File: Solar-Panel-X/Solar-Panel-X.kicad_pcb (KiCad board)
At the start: 6 copper layers, 48.4 x 48.4 mm, 81 parts, among them J1 FTS-105-01-L-DV-A, Q1 BSS138DWQ-7, Q2 MBT2222ADW1T1, Q3 BSS138DWQ-7, Q4 MBT2222ADW1T1, U1 BQ25570RGRR, U2 TSL2561

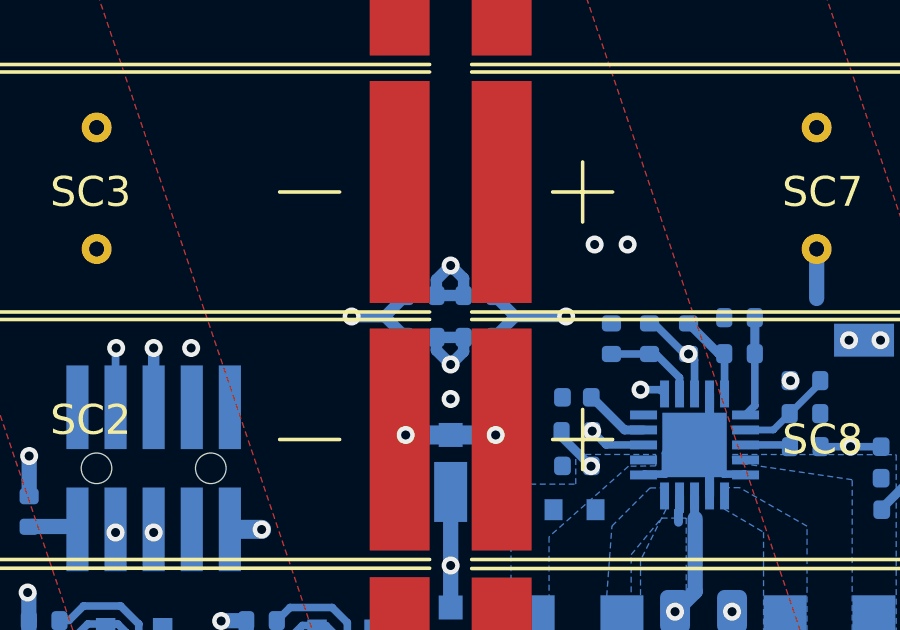
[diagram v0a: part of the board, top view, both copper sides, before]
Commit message: Modified coil resistor layout on X board
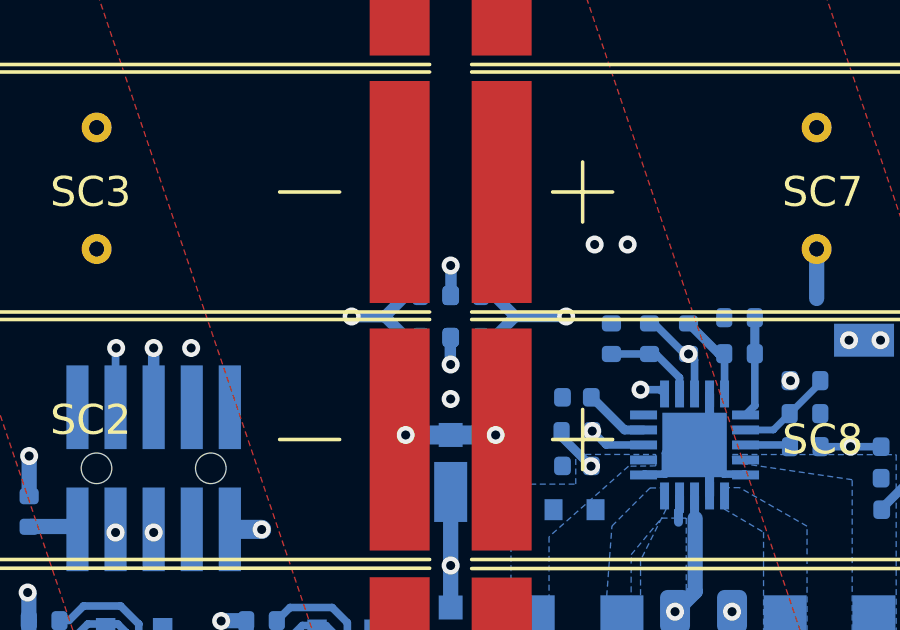
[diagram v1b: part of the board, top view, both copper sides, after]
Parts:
- moved R13 0.49 mm to (106.2, 67.0)
- moved R18 0.49 mm to (106.2, 65.6)
- moved R12 0.44 mm to (107.2, 67.0)
- moved R17 0.44 mm to (107.2, 65.6)
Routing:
- net COIL_N: track 17.1 -> 14.8 mm
- net COIL_P: track 17.3 -> 15.1 mm
- net /coil: track 13206.6 -> 13208.5 mm
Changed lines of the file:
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@@
   )
   (footprint "Resistor_SMD:R_0402_1005Metric" (layer "B.Cu")
-    (at 105.71397 65.6)
+    (at 106.2 65.6)
     (descr "Resistor SMD 0402 (1005 Metric), square (rectangular) end terminal, IPC_7351 nominal, (Body size source: IPC-SM-782 page 72, https://www.pcb-3d.com/wordpress/wp-content/uploads/ipc-sm-782a_amendment_1_and_2.pdf), generated with kicad-footprint-generator")
     (tags "resistor")
@@
   )
   (footprint "Resistor_SMD:R_0402_1005Metric" (layer "B.Cu")
-    (at 107.64225 65.6)
+    (at 107.2 65.6)
     (descr "Resistor SMD 0402 (1005 Metric), square (rectangular) end terminal, IPC_7351 nominal, (Body size source: IPC-SM-782 page 72, https://www.pcb-3d.com/wordpress/wp-content/uploads/ipc-sm-782a_amendment_1_and_2.pdf), generated with kicad-footprint-generator")
     (tags "resistor")
@@
   )
   (footprint "Resistor_SMD:R_0402_1005Metric" (layer "B.Cu")
-    (at 107.64225 66.997)
+    (at 107.2 67)
     (descr "Resistor SMD 0402 (1005 Metric), square (rectangular) end terminal, IPC_7351 nominal, (Body size source: IPC-SM-782 page 72, https://www.pcb-3d.com/wordpress/wp-content/uploads/ipc-sm-782a_amendment_1_and_2.pdf), generated with kicad-footprint-generator")
     (tags "resistor")
@@
   )
   (footprint "Resistor_SMD:R_0402_1005Metric" (layer "B.Cu")
-    (at 105.71397 66.997)
+    (at 106.2 66.997)
     (descr "Resistor SMD 0402 (1005 Metric), square (rectangular) end terminal, IPC_7351 nominal, (Body size source: IPC-SM-782 page 72, https://www.pcb-3d.com/wordpress/wp-content/uploads/ipc-sm-782a_amendment_1_and_2.pdf), generated with kicad-footprint-generator")
     (tags "resistor")
@@
   (segment (start 96.8 67.35) (end 96.8 66.7) (width 0.381) (layer "In2.Cu") (net 10))
   (segment (start 96.8 66.7) (end 98.9 64.6) (width 0.381) (layer "In2.Cu") (net 10))
-  (segment (start 106.22397 65.07603) (end 106.7 64.6) (width 0.381) (layer "B.Cu") (net 10))
-  (segment (start 106.22397 65.6) (end 107.13225 65.6) (width 0.381) (layer "B.Cu") (net 10))
+  (segment (start 106.71 64.61) (end 106.7 64.6) (width 0.1524) (layer "B.Cu") (net 10))
   (segment (start 96.8 67.35) (end 96.8 69.725) (width 0.381) (layer "B.Cu") (net 10))
-  (segment (start 106.7 64.6) (end 107.13225 65.03225) (width 0.381) (layer "B.Cu") (net 10))
-  (segment (start 107.13225 65.03225) (end 107.13225 65.6) (width 0.381) (layer "B.Cu") (net 10))
-  (segment (start 106.22397 65.6) (end 106.22397 65.07603) (width 0.381) (layer "B.Cu") (net 10))
+  (segment (start 106.71 65.6) (end 106.71 64.61) (width 0.381) (layer "B.Cu") (net 10))
   (via (at 106.7 67.9) (size 0.6) (drill 0.3) (layers "F.Cu" "B.Cu") (net 11))
   (via (at 96.8 73.5) (size 0.6) (drill 0.3) (layers "F.Cu" "B.Cu") (net 11))
@@
   (segment (start 99 67.9) (end 106.7 67.9) (width 0.381) (layer "In2.Cu") (net 11))
   (segment (start 96.8 73.5) (end 96.8 70.1) (width 0.381) (layer "In2.Cu") (net 11))
-  (segment (start 106.22397 66.997) (end 106.22397 67.42397) (width 0.381) (layer "B.Cu") (net 11))
-  (segment (start 106.22397 67.42397) (end 106.7 67.9) (width 0.381) (layer "B.Cu") (net 11))
-  (segment (start 107.13225 66.997) (end 107.13225 67.46775) (width 0.381) (layer "B.Cu") (net 11))
-  (segment (start 107.13225 67.46775) (end 106.7 67.9) (width 0.381) (layer "B.Cu") (net 11))
-  (segment (start 106.22397 66.997) (end 107.13225 66.997) (width 0.381) (layer "B.Cu") (net 11))
+  (segment (start 106.69 67.89) (end 106.7 67.9) (width 0.1524) (layer "B.Cu") (net 11))
+  (segment (start 106.69 67) (end 106.69 67.89) (width 0.381) (layer "B.Cu") (net 11))
   (segment (start 112.49644 70.081786) (end 111.408984 68.99433) (width 0.29972) (layer "B.Cu") (net 12))
   (segment (start 113.13 70.081786) (end 112.49644 70.081786) (width 0.29972) (layer "B.Cu") (net 12))
@@
   (segment (start 108.15525 66.997) (end 108.85225 66.3) (width 0.381) (layer "B.Cu") (net 22))
   (segment (start 103.4 66.3) (end 104.50397 66.3) (width 0.381) (layer "B.Cu") (net 22))
+  (segment (start 105.20397 66.997) (end 105.69 66.997) (width 0.381) (layer "B.Cu") (net 22))
   (segment (start 104.50397 66.3) (end 105.20397 65.6) (width 0.381) (layer "B.Cu") (net 22))
   (segment (start 103.4 66.3) (end 104.50697 66.3) (width 0.381) (layer "B.Cu") (net 22))
   (segment (start 108.85225 66.3) (end 110.55 66.3) (width 0.381) (layer "B.Cu") (net 22))
+  (segment (start 108.15225 65.6) (end 107.71 65.6) (width 0.381) (layer "B.Cu") (net 22))
+  (segment (start 105.20397 65.6) (end 105.69 65.6) (width 0.381) (layer "B.Cu") (net 22))
   (segment (start 104.50697 66.3) (end 105.20397 66.997) (width 0.381) (layer "B.Cu") (net 22))
+  (segment (start 107.713 66.997) (end 107.71 67) (width 0.381) (layer "B.Cu") (net 22))
   (segment (start 108.15225 65.6) (end 108.85225 66.3) (width 0.381) (layer "B.Cu") (net 22))
+  (segment (start 108.15525 66.997) (end 107.713 66.997) (width 0.381) (layer "B.Cu") (net 22))
   (via (at 106.7 74.6) (size 0.6) (drill 0.3) (layers "F.Cu" "B.Cu") (net 23))
   (via (at 91.3 74.6) (size 0.6) (drill 0.3) (layers "F.Cu" "B.Cu") (net 23))

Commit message: cleanup on X
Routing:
- net /coil: track 13208.5 -> 13203.6 mm
- net GND: track 28.3 -> 25.2 mm
- net Net-(D3-Pad1): track 14.4 -> 13.9 mm
